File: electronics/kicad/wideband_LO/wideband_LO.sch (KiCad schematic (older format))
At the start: 27 parts, among them U1 BFP620

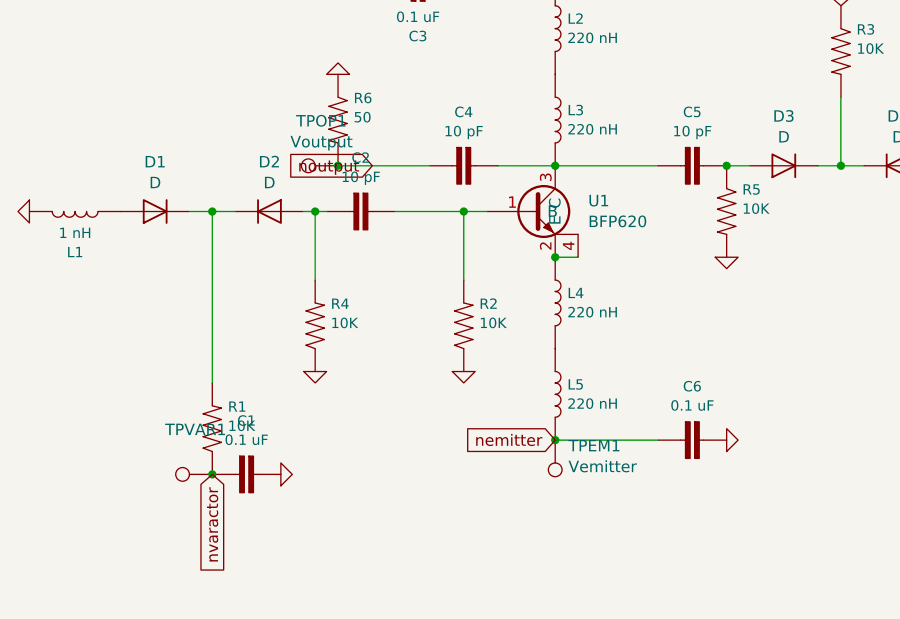
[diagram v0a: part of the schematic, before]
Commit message: Reduced pad size, found bug with FDTD, etc, etc.
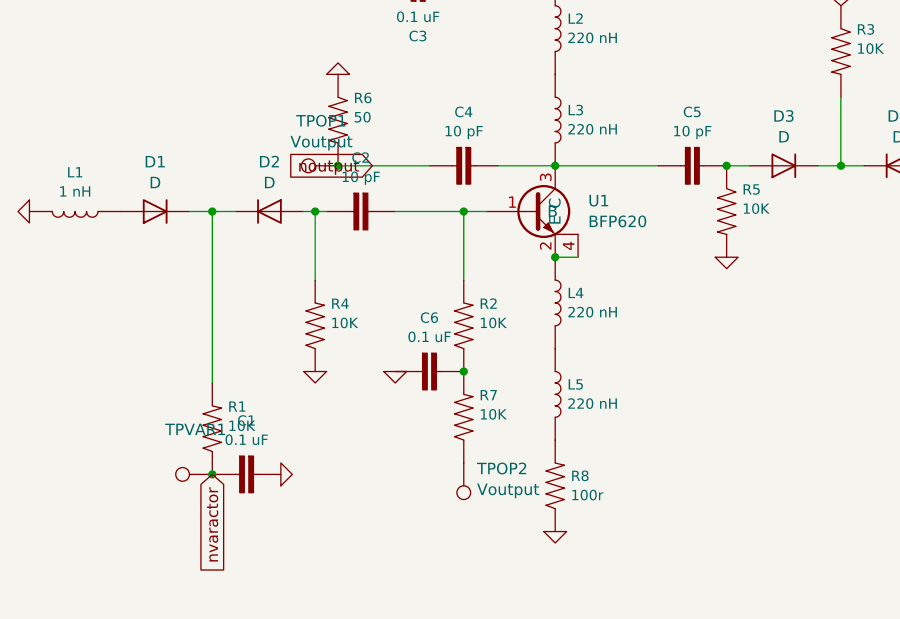
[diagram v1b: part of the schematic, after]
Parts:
- removed TPEM1: Vemitter, TestPoint:TestPoint_Pad_2.0x2.0mm, symbol Connector:Test_Point
- added R7: 10K, Resistor_SMD:R_0402_1005Metric, symbol SparkFun-Resistors:RESISTOR0402
- added R8: 100r, 0603, symbol SparkFun-Resistors:15OHM-0603-1_10W-1%
- added TPOP2: Voutput, TestPoint:TestPoint_Pad_1.5x1.5mm, symbol Connector:Test_Point
- C2, C4, C5: footprint 0402 -> Capacitor_SMD:C_0402_1005Metric
- L1, L2, L3, L4, L5, L6, R1, R2, R3, R4, R5, R6: footprint 0402 -> Resistor_SMD:R_0402_1005Metric
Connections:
- net GND: now also C6.2, R8.1; no longer C6.1, R2.1
- net nemitter: no longer names the net of L5.2
- net nemitter: now also R8.2; no longer C6.2
- new net: C6.1, R2.1, R7.2
- new net: R7.1, TPOP2.1
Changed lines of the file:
@@
 F 0 "R3" V 4655 2618 45  0000 L CNN
 F 1 "10K" V 4739 2618 45  0000 L CNN
-F 2 "0402" H 4750 2700 20  0001 C CNN
+F 2 "Resistor_SMD:R_0402_1005Metric" H 4750 2700 20  0001 C CNN
 F 3 "" H 4750 2550 60  0001 C CNN
 F 4 " " V 4834 2618 60  0000 L CNN "Field4"
@@
 F 0 "R1" V 2095 4132 45  0000 R CNN
 F 1 "10K" V 2011 4132 45  0000 R CNN
-F 2 "0402" H 2000 4350 20  0001 C CNN
+F 2 "Resistor_SMD:R_0402_1005Metric" H 2000 4350 20  0001 C CNN
 F 3 "" H 2000 4200 60  0001 C CNN
 F 4 " " V 1916 4132 60  0000 R CNN "Field4"
@@
 F 0 "L5" H 3553 4092 45  0000 L CNN
 F 1 "220 nH" H 3553 4008 45  0000 L CNN
-F 2 "0402" H 3500 4300 20  0001 C CNN
+F 2 "Resistor_SMD:R_0402_1005Metric" H 3500 4300 20  0001 C CNN
 F 3 "" H 3500 4050 50  0001 C CNN
 F 4 "" H 3552 3966 60  0000 L CNN "Field4"
@@
 F 0 "L4" H 3553 3692 45  0000 L CNN
 F 1 "220 nH" H 3553 3608 45  0000 L CNN
-F 2 "0402" H 3500 3900 20  0001 C CNN
+F 2 "Resistor_SMD:R_0402_1005Metric" H 3500 3900 20  0001 C CNN
 F 3 "" H 3500 3650 50  0001 C CNN
 F 4 "" H 3552 3566 60  0000 L CNN "Field4"
@@
 	3500 3450 3600 3450
 Connection ~ 3500 3450
-$Comp
-L SparkFun-Resistors:RESISTOR0402 R2
-U 1 1 5EE2D2F4
-P 3100 3750
-F 0 "R2" V 3195 3682 45  0000 R CNN
-F 1 "10K" V 3111 3682 45  0000 R CNN
-F 2 "0402" H 3100 3900 20  0001 C CNN
-F 3 "" H 3100 3750 60  0001 C CNN
-F 4 " " V 3016 3682 60  0000 R CNN "Field4"
-	1    3100 3750
-	0    -1   -1   0
-$EndComp
 Wire Wire Line
 	3100 3550 3100 3250
 Connection ~ 3100 3250
-$Comp
-L power:GND #PWR0103
-U 1 1 5EE2EA29
-P 3100 3950
-F 0 "#PWR0103" H 3100 3950 30  0001 C CNN
-F 1 "GND" H 3100 3880 30  0001 C CNN
-F 2 "" H 3100 3950 50  0001 C CNN
-F 3 "" H 3100 3950 50  0001 C CNN
-	1    3100 3950
-	1    0    0    -1
-$EndComp
-$Comp
-L Connector:Test_Point TPEM1
-U 1 1 5EE3076A
-P 3500 4250
-F 0 "TPEM1" H 3442 4276 50  0000 R CNN
-F 1 "Vemitter" H 3442 4367 50  0000 R CNN
-F 2 "TestPoint:TestPoint_Pad_2.0x2.0mm" H 3700 4250 50  0001 C CNN
-F 3 "~" H 3700 4250 50  0001 C CNN
-F 4 "V" H 3500 4250 50  0001 C CNN "Spice_Primitive"
-F 5 "dc -2" H 3500 4250 50  0001 C CNN "Spice_Model"
-F 6 "N" H 3500 4250 50  0001 C CNN "Spice_Netlist_Enabled"
-	1    3500 4250
-	-1   0    0    1
-$EndComp
-$Comp
-L SparkFun-Capacitors:4.7UF0603 C6
-U 1 1 5EE32EB3
-P 4050 4250
-F 0 "C6" V 3816 4300 45  0000 C CNN
-F 1 "0.1 uF" V 3900 4300 45  0000 C CNN
-F 2 "0603" H 4050 4500 20  0001 C CNN
-F 3 "" H 4050 4250 50  0001 C CNN
-F 4 "" H 4158 4216 60  0000 L CNN "Field4"
-	1    4050 4250
-	0    1    1    0
-$EndComp
-Wire Wire Line
-	3950 4250 3500 4250
-Connection ~ 3500 4250
 $Comp
 L Connector:Test_Point TPOP1
@@
 L power:GND #PWR0105
 U 1 1 5EE3FB1C
-P 4250 4250
-F 0 "#PWR0105" H 4250 4250 30  0001 C CNN
-F 1 "GND" H 4250 4180 30  0001 C CNN
-F 2 "" H 4250 4250 50  0001 C CNN
-F 3 "" H 4250 4250 50  0001 C CNN
-	1    4250 4250
-	0    -1   -1   0
+P 3500 4650
+F 0 "#PWR0105" H 3500 4650 30  0001 C CNN
+F 1 "GND" H 3500 4580 30  0001 C CNN
+F 2 "" H 3500 4650 50  0001 C CNN
+F 3 "" H 3500 4650 50  0001 C CNN
+	1    3500 4650
+	1    0    0    -1
 $EndComp
 $Comp
@@
 F 0 "C4" V 2816 3100 45  0000 C CNN
 F 1 "10 pF" V 2900 3100 45  0000 C CNN
-F 2 "0402" H 3050 3300 20  0001 C CNN
+F 2 "Capacitor_SMD:C_0402_1005Metric" H 3050 3300 20  0001 C CNN
 F 3 "" H 3050 3050 50  0001 C CNN
 F 4 "" H 3158 3016 60  0000 L CNN "Field4"
@@
 F 0 "R4" V 2545 3682 45  0000 R CNN
 F 1 "10K" V 2461 3682 45  0000 R CNN
-F 2 "0402" H 2450 3900 20  0001 C CNN
+F 2 "Resistor_SMD:R_0402_1005Metric" H 2450 3900 20  0001 C CNN
 F 3 "" H 2450 3750 60  0001 C CNN
 F 4 " " V 2366 3682 60  0000 R CNN "Field4"
@@
 U 1 1 5EE21BFD
 P 1400 3250
-F 0 "L1" V 1579 3250 45  0000 C CNN
-F 1 "1 nH" V 1495 3250 45  0000 C CNN
-F 2 "0402" H 1400 3500 20  0001 C CNN
+F 0 "L1" V 1230 3250 45  0000 C CNN
+F 1 "1 nH" V 1314 3250 45  0000 C CNN
+F 2 "Resistor_SMD:R_0402_1005Metric" H 1400 3500 20  0001 C CNN
 F 3 "" H 1400 3250 50  0001 C CNN
 F 4 "" H 1452 3166 60  0000 L CNN "Field4"
@@
 F 0 "C5" V 3816 3100 45  0000 C CNN
 F 1 "10 pF" V 3900 3100 45  0000 C CNN
-F 2 "0402" H 4050 3300 20  0001 C CNN
+F 2 "Capacitor_SMD:C_0402_1005Metric" H 4050 3300 20  0001 C CNN
 F 3 "" H 4050 3050 50  0001 C CNN
 F 4 "" H 4158 3016 60  0000 L CNN "Field4"
@@
 F 0 "C2" V 2366 3300 45  0000 C CNN
 F 1 "10 pF" V 2450 3300 45  0000 C CNN
-F 2 "0402" H 2600 3500 20  0001 C CNN
+F 2 "Capacitor_SMD:C_0402_1005Metric" H 2600 3500 20  0001 C CNN
 F 3 "" H 2600 3250 50  0001 C CNN
 F 4 "" H 2708 3216 60  0000 L CNN "Field4"
@@
 F 0 "R6" V 2455 2918 45  0000 L CNN
 F 1 "50" V 2539 2918 45  0000 L CNN
-F 2 "0402" H 2550 3000 20  0001 C CNN
+F 2 "Resistor_SMD:R_0402_1005Metric" H 2550 3000 20  0001 C CNN
 F 3 "" H 2550 2850 60  0001 C CNN
 F 4 " " V 2634 2918 60  0000 L CNN "Field4"
@@
 F 0 "L2" H 3553 2492 45  0000 L CNN
 F 1 "220 nH" H 3553 2408 45  0000 L CNN
-F 2 "0402" H 3500 2700 20  0001 C CNN
+F 2 "Resistor_SMD:R_0402_1005Metric" H 3500 2700 20  0001 C CNN
 F 3 "" H 3500 2450 50  0001 C CNN
 F 4 "" H 3552 2366 60  0000 L CNN "Field4"
@@
 F 0 "L3" H 3553 2892 45  0000 L CNN
 F 1 "220 nH" H 3553 2808 45  0000 L CNN
-F 2 "0402" H 3500 3100 20  0001 C CNN
+F 2 "Resistor_SMD:R_0402_1005Metric" H 3500 3100 20  0001 C CNN
 F 3 "" H 3500 2850 50  0001 C CNN
 F 4 "" H 3552 2766 60  0000 L CNN "Field4"
@@
 F 0 "R5" V 4155 3318 45  0000 L CNN
 F 1 "10K" V 4239 3318 45  0000 L CNN
-F 2 "0402" H 4250 3400 20  0001 C CNN
+F 2 "Resistor_SMD:R_0402_1005Metric" H 4250 3400 20  0001 C CNN
 F 3 "" H 4250 3250 60  0001 C CNN
 F 4 " " V 4334 3318 60  0000 L CNN "Field4"
@@
 F 0 "L6" V 5529 3050 45  0000 C CNN
 F 1 "1 nH" V 5445 3050 45  0000 C CNN
-F 2 "0402" H 5350 3300 20  0001 C CNN
+F 2 "Resistor_SMD:R_0402_1005Metric" H 5350 3300 20  0001 C CNN
 F 3 "" H 5350 3050 50  0001 C CNN
 F 4 "" H 5402 2966 60  0000 L CNN "Field4"
@@
 Text GLabel 2700 3050 0    50   Input ~ 0
 noutput
-Text GLabel 3500 4250 0    50   Input ~ 0
-nemitter
 Connection ~ 2000 4400
 Text GLabel 2000 4400 3    50   Input ~ 0
@@
 Text GLabel 4750 2350 1    50   Input ~ 0
 nvaractor
+$Comp
+L SparkFun-Resistors:RESISTOR0402 R2
+U 1 1 5EE2D2F4
+P 3100 3750
+F 0 "R2" V 3195 3682 45  0000 R CNN
+F 1 "10K" V 3111 3682 45  0000 R CNN
+F 2 "Resistor_SMD:R_0402_1005Metric" H 3100 3900 20  0001 C CNN
+F 3 "" H 3100 3750 60  0001 C CNN
+F 4 " " V 3016 3682 60  0000 R CNN "Field4"
+	1    3100 3750
+	0    -1   -1   0
+$EndComp
+$Comp
+L Connector:Test_Point TPOP2
+U 1 1 5EF2155B
+P 3100 4350
+F 0 "TPOP2" H 3042 4376 50  0000 R CNN
+F 1 "Voutput" H 3042 4467 50  0000 R CNN
+F 2 "TestPoint:TestPoint_Pad_1.5x1.5mm" H 3300 4350 50  0001 C CNN
+F 3 "~" H 3300 4350 50  0001 C CNN
+F 4 "R" H 3100 4350 50  0001 C CNN "Spice_Primitive"
+F 5 "100M" H 3100 4350 50  0001 C CNN "Spice_Model"
+F 6 "N" H 3100 4350 50  0001 C CNN "Spice_Netlist_Enabled"
+	1    3100 4350
+	-1   0    0    1
+$EndComp
+$Comp
+L SparkFun-Capacitors:4.7UF0603 C6
+U 1 1 5EF2A408
+P 2900 3950
+F 0 "C6" V 2666 4000 45  0000 C CNN
+F 1 "0.1 uF" V 2750 4000 45  0000 C CNN
+F 2 "0603" H 2900 4200 20  0001 C CNN
+F 3 "" H 2900 3950 50  0001 C CNN
+F 4 "" H 3008 3916 60  0000 L CNN "Field4"
+	1    2900 3950
+	0    1    1    0
+$EndComp
+$Comp
+L power:GND #PWR0103
+U 1 1 5EF2B7C8
+P 2800 3950
+F 0 "#PWR0103" H 2800 3950 30  0001 C CNN
+F 1 "GND" H 2800 3880 30  0001 C CNN
+F 2 "" H 2800 3950 50  0001 C CNN
+F 3 "" H 2800 3950 50  0001 C CNN
+	1    2800 3950
+	1    0    0    -1
+$EndComp
+$Comp
+L SparkFun-Resistors:RESISTOR0402 R7
+U 1 1 5EF3ECA2
+P 3100 4150
+F 0 "R7" V 3195 4082 45  0000 R CNN
+F 1 "10K" V 3111 4082 45  0000 R CNN
+F 2 "Resistor_SMD:R_0402_1005Metric" H 3100 4300 20  0001 C CNN
+F 3 "" H 3100 4150 60  0001 C CNN
+F 4 " " V 3016 4082 60  0000 R CNN "Field4"
+	1    3100 4150
+	0    -1   -1   0
+$EndComp
+Connection ~ 3100 3950
+$Comp
+L SparkFun-Resistors:15OHM-0603-1_10W-1% R8
+U 1 1 5EF4BB1B
+P 3500 4450
+F 0 "R8" V 3542 4382 45  0000 R CNN
+F 1 "100r" V 3458 4382 45  0000 R CNN
+F 2 "0603" H 3500 4600 20  0001 C CNN
+F 3 "" H 3500 4450 60  0001 C CNN
+F 4 "" V 3416 4382 60  0000 R CNN "Field4"
+	1    3500 4450
+	0    -1   -1   0
+$EndComp
 $EndSCHEMATC

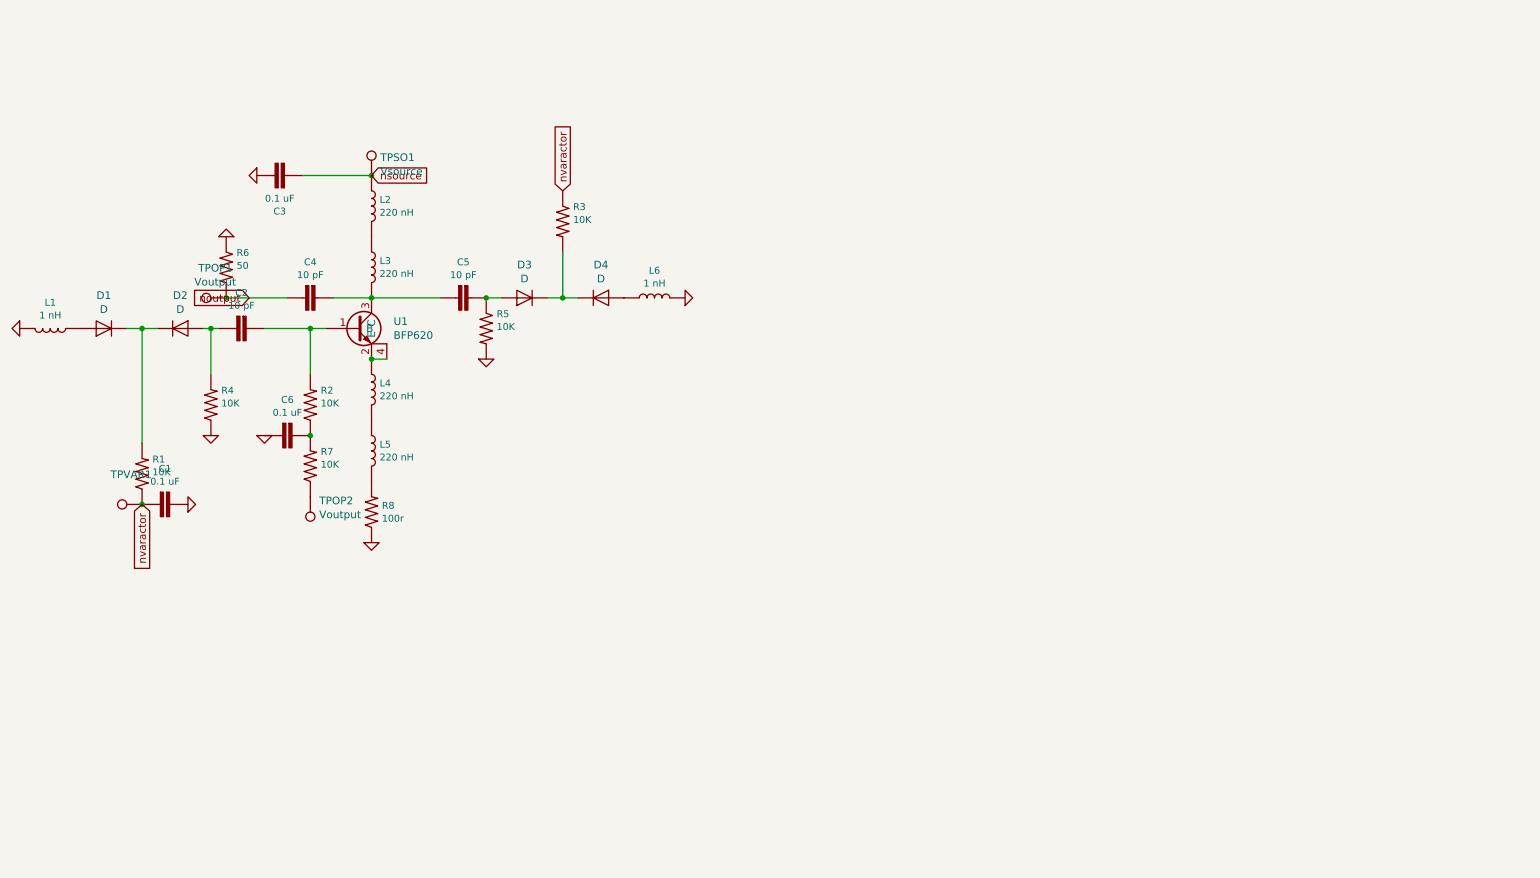
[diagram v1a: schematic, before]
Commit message: Buck-boost to linear
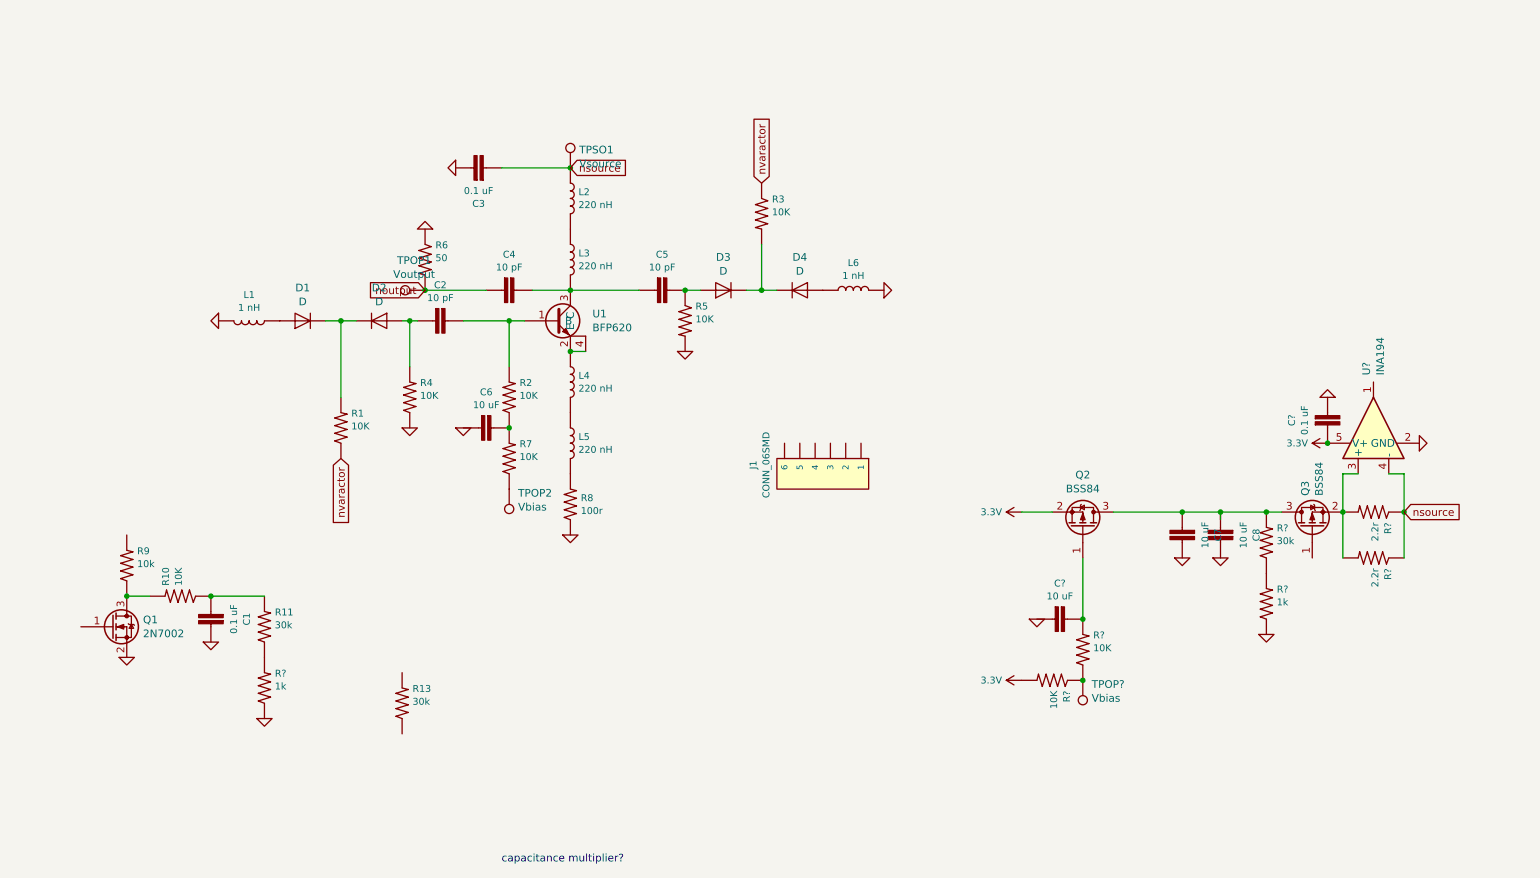
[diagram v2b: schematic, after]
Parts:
- removed TPVAR1: (no value), TestPoint:TestPoint_Pad_1.5x1.5mm, symbol Connector:Test_Point
- added C7, C8, C?: 10 uF, 0603, symbol SparkFun-Capacitors:4.7UF0603
- added C?: 0.1 uF, 0603, symbol SparkFun-Capacitors:4.7UF0603
- added J1: CONN_06SMD, 1X06-SMD_RA_MALE, symbol SparkFun-Connectors:CONN_06SMD
- added Q1: 2N7002, Package_TO_SOT_SMD:SOT-23, symbol Transistor_FET:BSS138
- added Q2, Q3: BSS84, Package_TO_SOT_SMD:SOT-23, symbol Transistor_FET:BSS84
- added R10, R? (x2): 10K, Resistor_SMD:R_0402_1005Metric, symbol SparkFun-Resistors:RESISTOR0402
- added R11, R?: 30k, Resistor_SMD:R_0603_1608Metric, symbol SparkFun-Resistors:RESISTOR0402
- added R13: 30k, Resistor_SMD:R_0402_1005Metric, symbol SparkFun-Resistors:RESISTOR0402
- added R9: 10k, Resistor_SMD:R_0603_1608Metric, symbol SparkFun-Resistors:0.05OHM-0603-1_5W-1%
- added R? (x2): 2.2r, Resistor_SMD:R_0805_2012Metric, symbol SparkFun-Resistors:RESISTOR0402
- added R? (x2): 1k, Resistor_SMD:R_0603_1608Metric, symbol SparkFun-Resistors:RESISTOR0402
- added TPOP?: Vbias, TestPoint:TestPoint_Pad_1.5x1.5mm, symbol Connector:Test_Point
- added U?: INA194, Package_TO_SOT_SMD:SOT-23-5, symbol Amplifier_Current:INA194
- C6: value 0.1 uF -> 10 uF
- TPOP2: value Voutput -> Vbias
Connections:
- net labels added: 3.3V
- wire segments 18 -> 33
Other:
- note added: "capacitance multiplier?\n"
- moved on the sheet: C1, C2, C3, C4, C5, C6, D1, D2, D3, D4, L1, L2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

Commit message: Backup
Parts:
- removed R13: 30k, Resistor_SMD:R_0402_1005Metric, symbol SparkFun-Resistors:RESISTOR0402
- added C11: 0.1 uF, 0603, symbol SparkFun-Capacitors:4.7UF0603
- added R12: 10K, Resistor_SMD:R_0402_1005Metric, symbol SparkFun-Resistors:RESISTOR0402
- added TPOP3, TPOP7, TPOP8: Vbias, TestPoint:TestPoint_Pad_1.5x1.5mm, symbol Connector:Test_Point
- added TPOP4, TPOP5: 48V, TestPoint:TestPoint_Pad_1.5x1.5mm, symbol Connector:Test_Point
- added TPOP9: varactor, TestPoint:TestPoint_Pad_1.5x1.5mm, symbol Connector:Test_Point
- C1: value 0.1 uF -> 10 uF
- J1: Field4 (none) -> CONN-08971
- R10: value 10K -> 1k
- R14: renamed from R?; value 10K -> 1K
- R9: value 10k -> 30k
- gave numbers to parts that had none: 10
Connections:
- wire segments 33 -> 36
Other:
- note removed: "capacitance multiplier?\n"
- moved on the sheet: C10, C7, C8, C9, Q1, Q2, Q3, R10, R11, R13, R14, R15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
